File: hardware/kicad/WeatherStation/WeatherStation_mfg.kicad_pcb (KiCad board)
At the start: 4 copper layers, 100 x 80 mm, 124 parts, among them J1 USB-C, J10 SOIL_TEMP, J11 LEAF_WET, J12 PYRANOMETER, J13 PANEL_TEMP_F, J14 PANEL_TEMP_B, J15 POWER_PULSE, J16 RS485_Bus, J18 SMA_WiFi, J19 RJ45_Magjack, J2 SOLAR_IN, J20 NanoSIM, J21 SMA_LTE, J22 MicroSD, J3 BATTERY, J4 ANEMOMETER, J5 RAIN_GAUGE, J6 SMA_LoRa, J7 DEBUG_UART, J8 SOIL_MOIST_1, J9 SOIL_MOIST_2, Q1 FS8205A, SW1 BOOT, SW2 RESET, SW3 MODE_DIP, U10 STM32F407VGT6, U11 MAX3485ESA+, U12 ATWINC1500, U13 RN4870-I/RM, U14 W5500, U15 SIM7600E-H, U16 TPS7A2033, U2 TP4056, U2A DW01A, U3 AMS1117-3.3, U4 BME280, U5 AS5600, U6 SI1145, U7 BH1750FVI, U8 SX1276/RFM95W, Y1 8MHz, Y2 25MHz

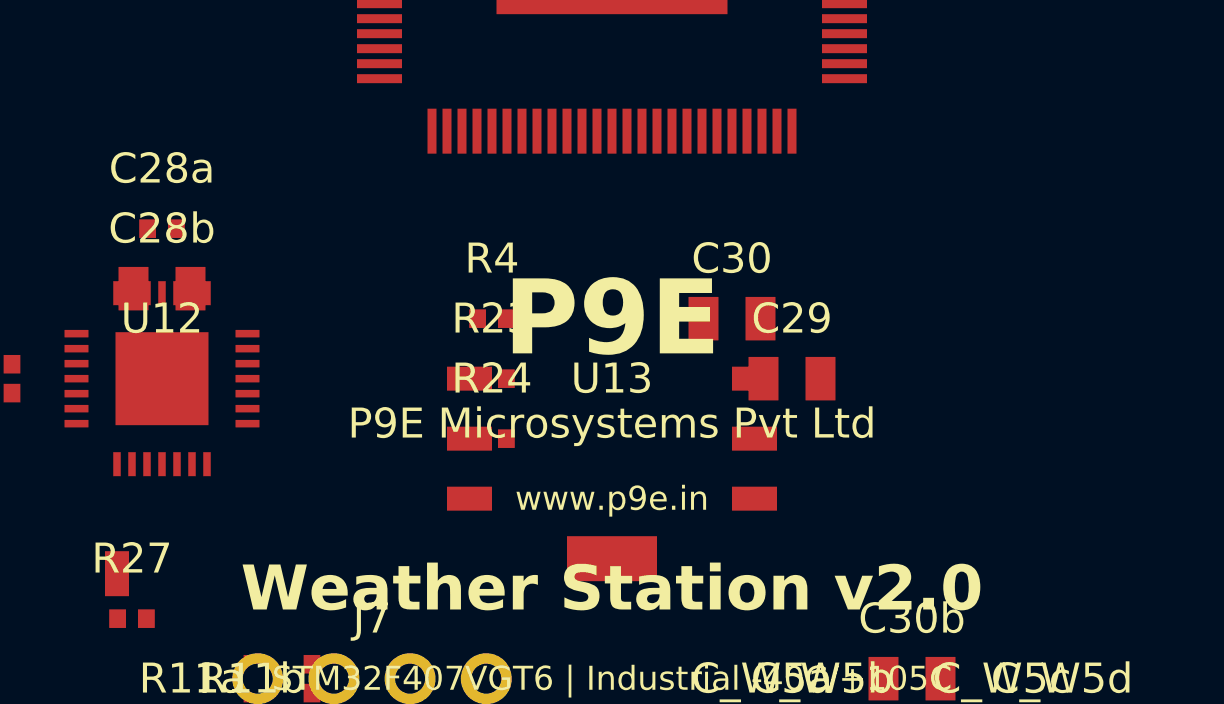
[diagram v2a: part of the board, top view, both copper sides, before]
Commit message: style: apply P9E 3-line label format on front and back silkscreen
Front silkscreen (F.SilkS) — 3-line P9E label block:
  Line 1: P9E              (3.5mm bold, company mark)
  Line 2: P9E Microsystems Pvt Ltd  (1.2mm bold, full name)
  Line 3: www.p9e.in       (1.0mm, website)

Product info kept separate below the label block:
  Weather Station v2.0 | STM32F407VGT6 | Industrial -40C/+105C

Back silkscreen (B.SilkS) — matching 3-line P9E label:
  P9E / P9E Microsystems Pvt Ltd / www.p9e.in
  Plus regulatory info: Rev 2.0, 4-Layer, ENIG, RoHS, IPC Class 2

Applied consistently to both WeatherStation.kicad_pcb (outline)
and WeatherStation_mfg.kicad_pcb (manufacturing).

https://claude.ai/code/session_01XHnfZQ5BbxTCTBMCteQyVe
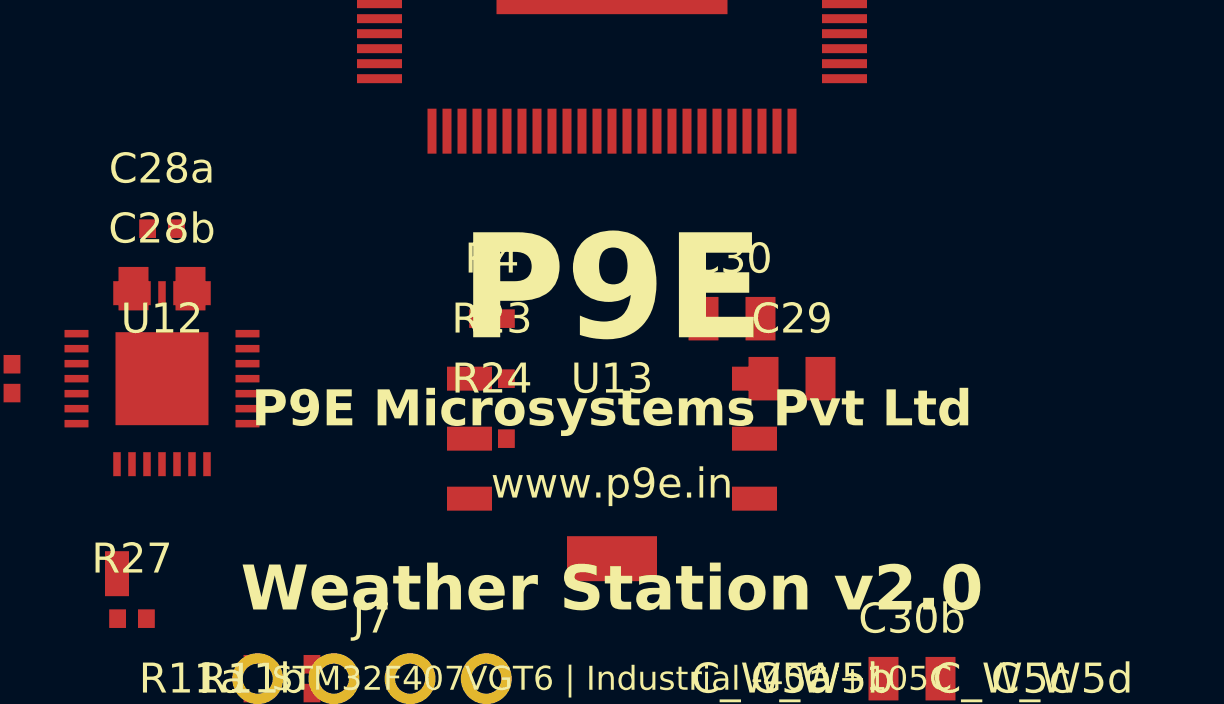
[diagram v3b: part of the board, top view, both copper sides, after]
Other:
- board text added: "P9E P9E Microsystems Pvt Ltd www.p9e.in"
- board text added: "Weather Station PCB Rev 2.0 4-Layer | FR4 Tg170 | ENIG RoHS Compliant | IPC Class 2 Conformal coat before deployment"
- board text removed: "P9E Microsystems Pvt Ltd www.p9e.in Weather Station PCB Rev 2.0 4-Layer | FR4 Tg170 | ENIG RoHS Compliant | IPC Class 2 Conformal coat before deployment"
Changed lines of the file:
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@@
   ;; SILKSCREEN
   ;; =====================================================================
-  (gr_text "P9E" (at 50 36) (layer "F.SilkS")
-    (effects (font (size 2.5 2.5) (thickness 0.3) (bold yes)) (justify center))
+  ;; P9E 3-Line Label — Front silkscreen (centered on board)
+  (gr_text "P9E" (at 50 35) (layer "F.SilkS")
+    (effects (font (size 3.5 3.5) (thickness 0.4) (bold yes)) (justify center))
   )
-  (gr_text "P9E Microsystems Pvt Ltd" (at 50 39.5) (layer "F.SilkS")
+  (gr_text "P9E Microsystems Pvt Ltd" (at 50 39) (layer "F.SilkS")
+    (effects (font (size 1.2 1.2) (thickness 0.18) (bold yes)) (justify center))
+  )
+  (gr_text "www.p9e.in" (at 50 41.5) (layer "F.SilkS")
     (effects (font (size 1 1) (thickness 0.15)) (justify center))
   )
-  (gr_text "www.p9e.in" (at 50 42) (layer "F.SilkS")
-    (effects (font (size 0.8 0.8) (thickness 0.12)) (justify center))
-  )
+  ;; Product info (below P9E label)
   (gr_text "Weather Station v2.0" (at 50 45) (layer "F.SilkS")
     (effects (font (size 1.5 1.5) (thickness 0.2) (bold yes)) (justify center))
@@
     (effects (font (size 0.8 0.8) (thickness 0.12)) (justify center))
   )
-  ;; Back silkscreen
-  (gr_text "P9E Microsystems Pvt Ltd\nwww.p9e.in\nWeather Station PCB Rev 2.0\n4-Layer | FR4 Tg170 | ENIG\nRoHS Compliant | IPC Class 2\nConformal coat before deployment" (at 50 40) (layer "B.SilkS")
+  ;; P9E 3-Line Label — Back silkscreen
+  (gr_text "P9E\nP9E Microsystems Pvt Ltd\nwww.p9e.in" (at 50 35) (layer "B.SilkS")
+    (effects (font (size 1.5 1.5) (thickness 0.2) (bold yes)) (justify center mirror))
+  )
+  ;; Back silkscreen — regulatory/specs
+  (gr_text "Weather Station PCB Rev 2.0\n4-Layer | FR4 Tg170 | ENIG\nRoHS Compliant | IPC Class 2\nConformal coat before deployment" (at 50 44) (layer "B.SilkS")
     (effects (font (size 1 1) (thickness 0.15)) (justify center mirror))
   )
